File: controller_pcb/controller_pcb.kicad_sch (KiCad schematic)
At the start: 7 parts, among them J1 ARM-JTAG-10, J2 12402012E212A, U1 STM32G070RBTx

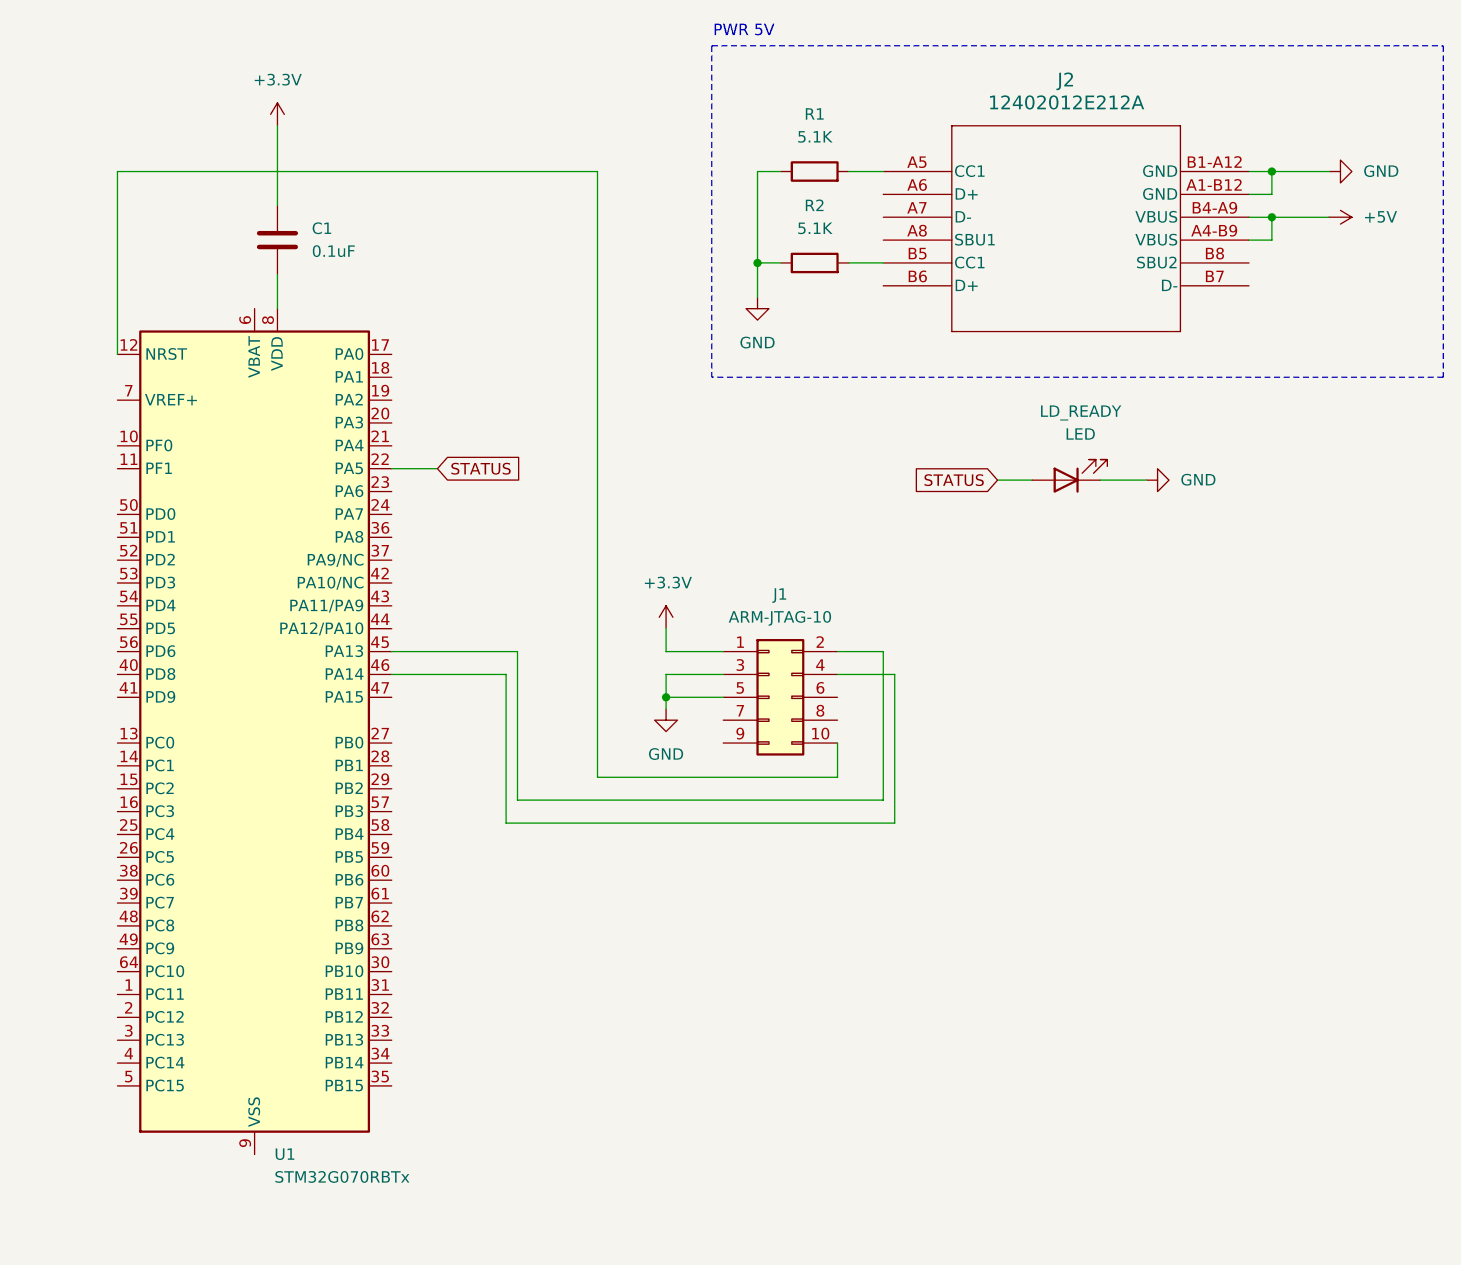
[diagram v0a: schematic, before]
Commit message: kicad: add status LED
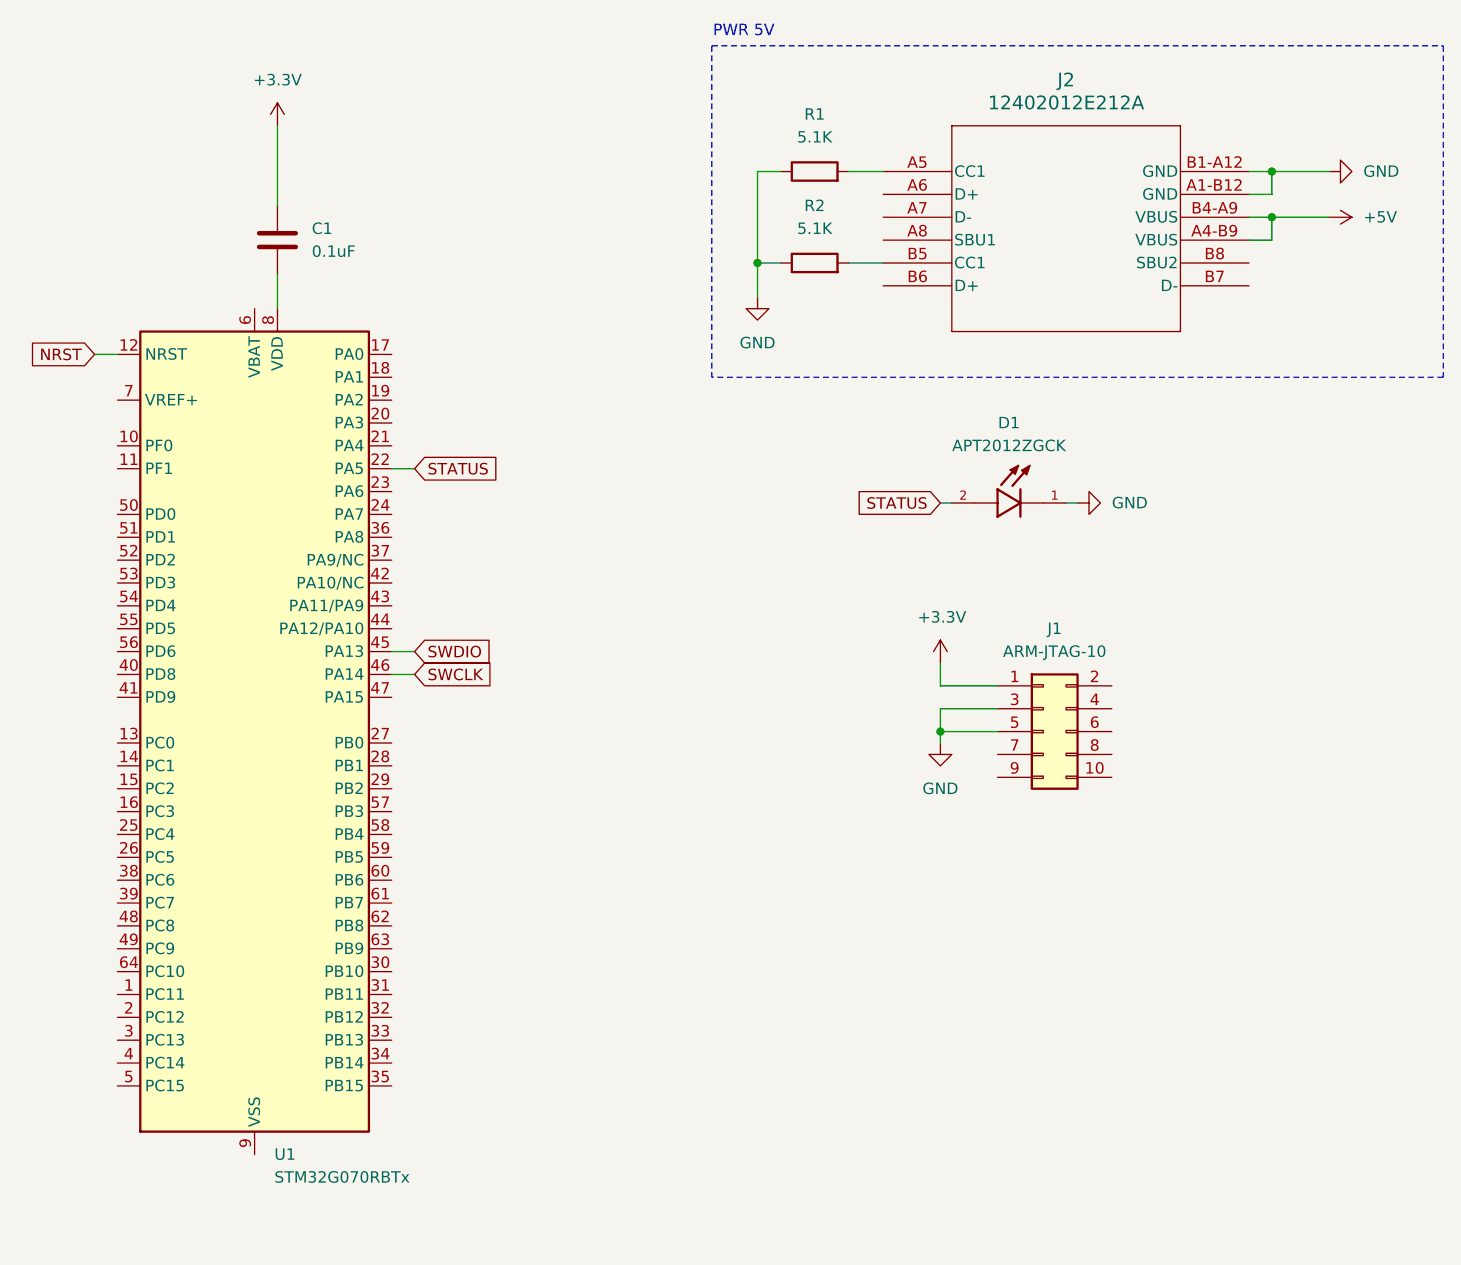
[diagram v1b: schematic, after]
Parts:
- removed LD_READY: LED, symbol Device:LED
- added D1: APT2012ZGCK, APT2012ZGCK:LED_APT2012ZGCK, symbol APT2012ZGCK:APT2012ZGCK
- J1: footprint (none) -> Connector_PinHeader_1.27mm:PinHeader_2x05_P1.27mm_Vertical
- J2: footprint 12402012E212A_AMP -> vendor_eda:12402012E212A_AMP
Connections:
- net GND: now also D1.1
- net STATUS: now also D1.2
- net at J1.10 (Pin_10): no longer U1.12 (NRST)
- net at J1.2 (Pin_2): no longer U1.45 (PA13)
- net at J1.4 (Pin_4): no longer U1.46 (PA14)
- new net NRST: U1.12 (NRST)
- new net SWCLK: U1.46 (PA14)
- new net SWDIO: U1.45 (PA13)
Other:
- moved on the sheet: J1

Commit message: chore: refactor gpio utils
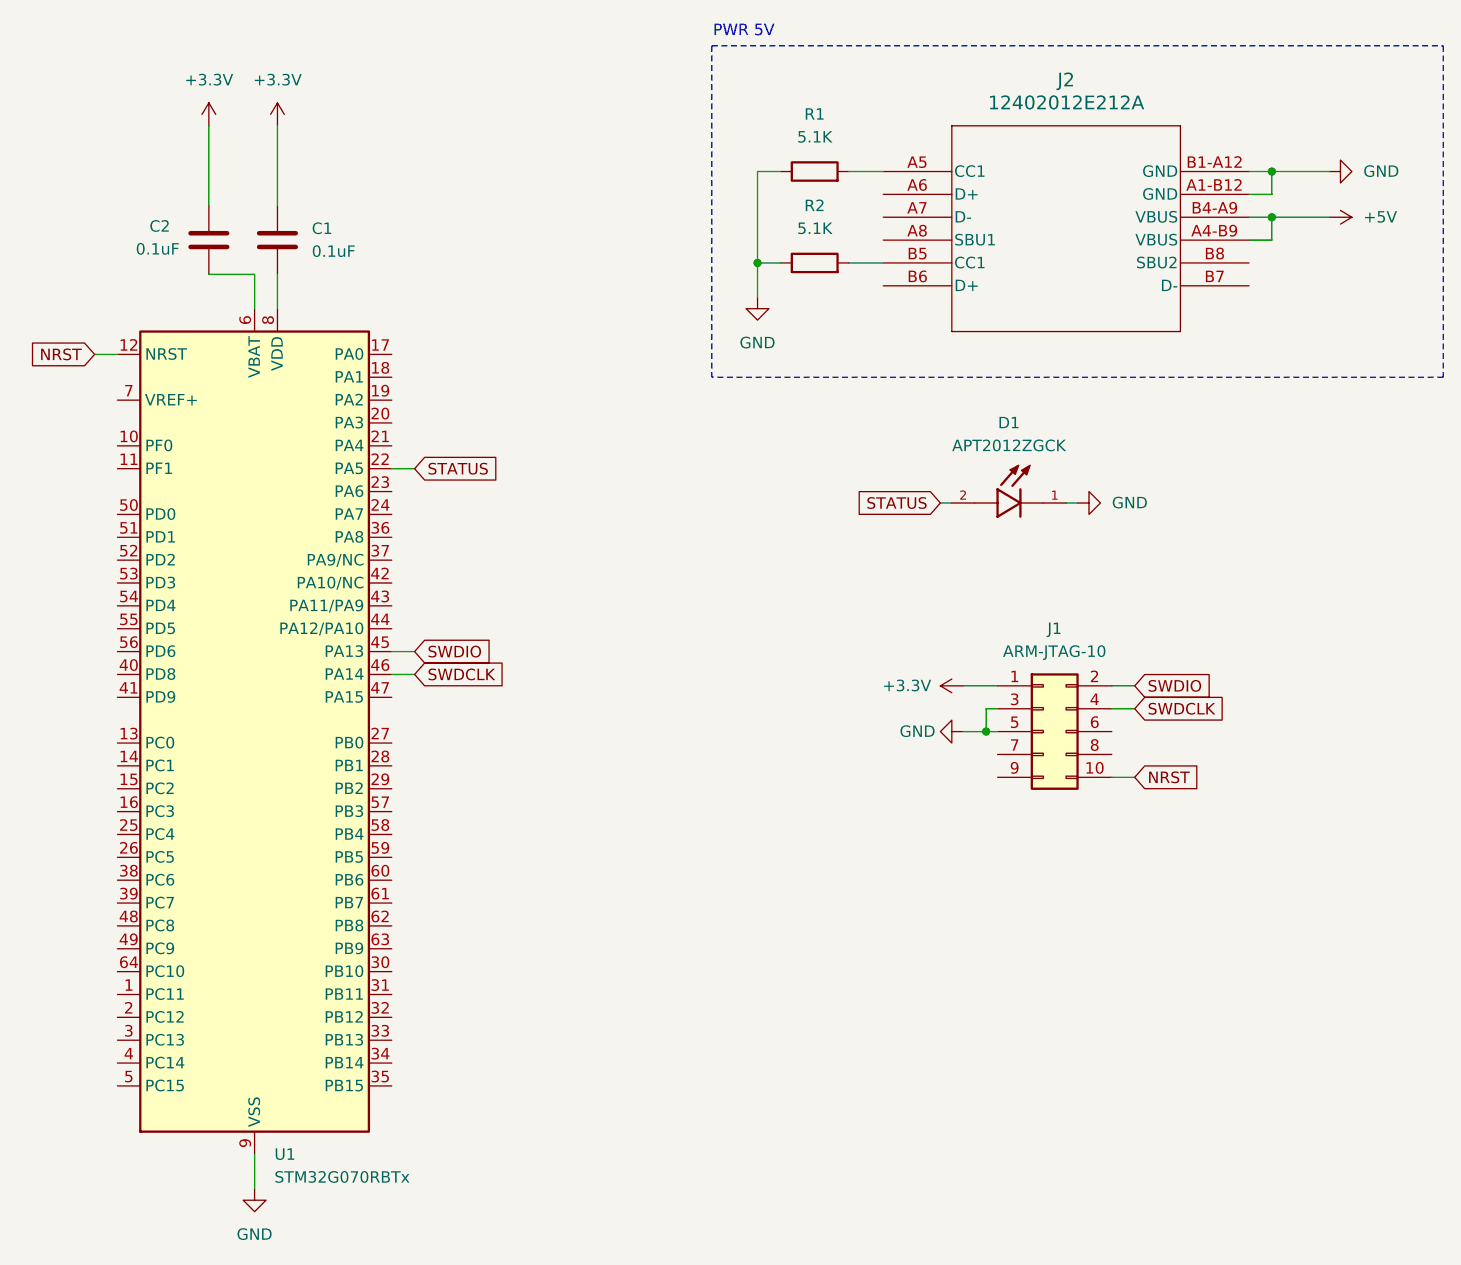
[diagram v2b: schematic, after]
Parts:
- added C2: 0.1uF, symbol Device:C
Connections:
- net SWCLK is gone; now on net SWDCLK: U1.46 (PA14)
- net +3.3V: now also C2.1
- net GND: now also U1.9 (VSS)
- net NRST: now also J1.10 (Pin_10)
- net SWDIO: now also J1.2 (Pin_2)
- net at U1.6 (VBAT): now also C2.2
- net SWDCLK: now reaches J1.4 (Pin_4)
